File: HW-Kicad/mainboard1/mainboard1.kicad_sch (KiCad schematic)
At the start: 11 parts, among them J1 Conn_01x02_Male, J2 Conn_01x02_Male, J3 Conn_01x07_Male, J4 Conn_01x04_Male, J5 Conn_01x04_Male, U1 MCP1700-2802E_TO92, U2 ESP32-WROOM-E

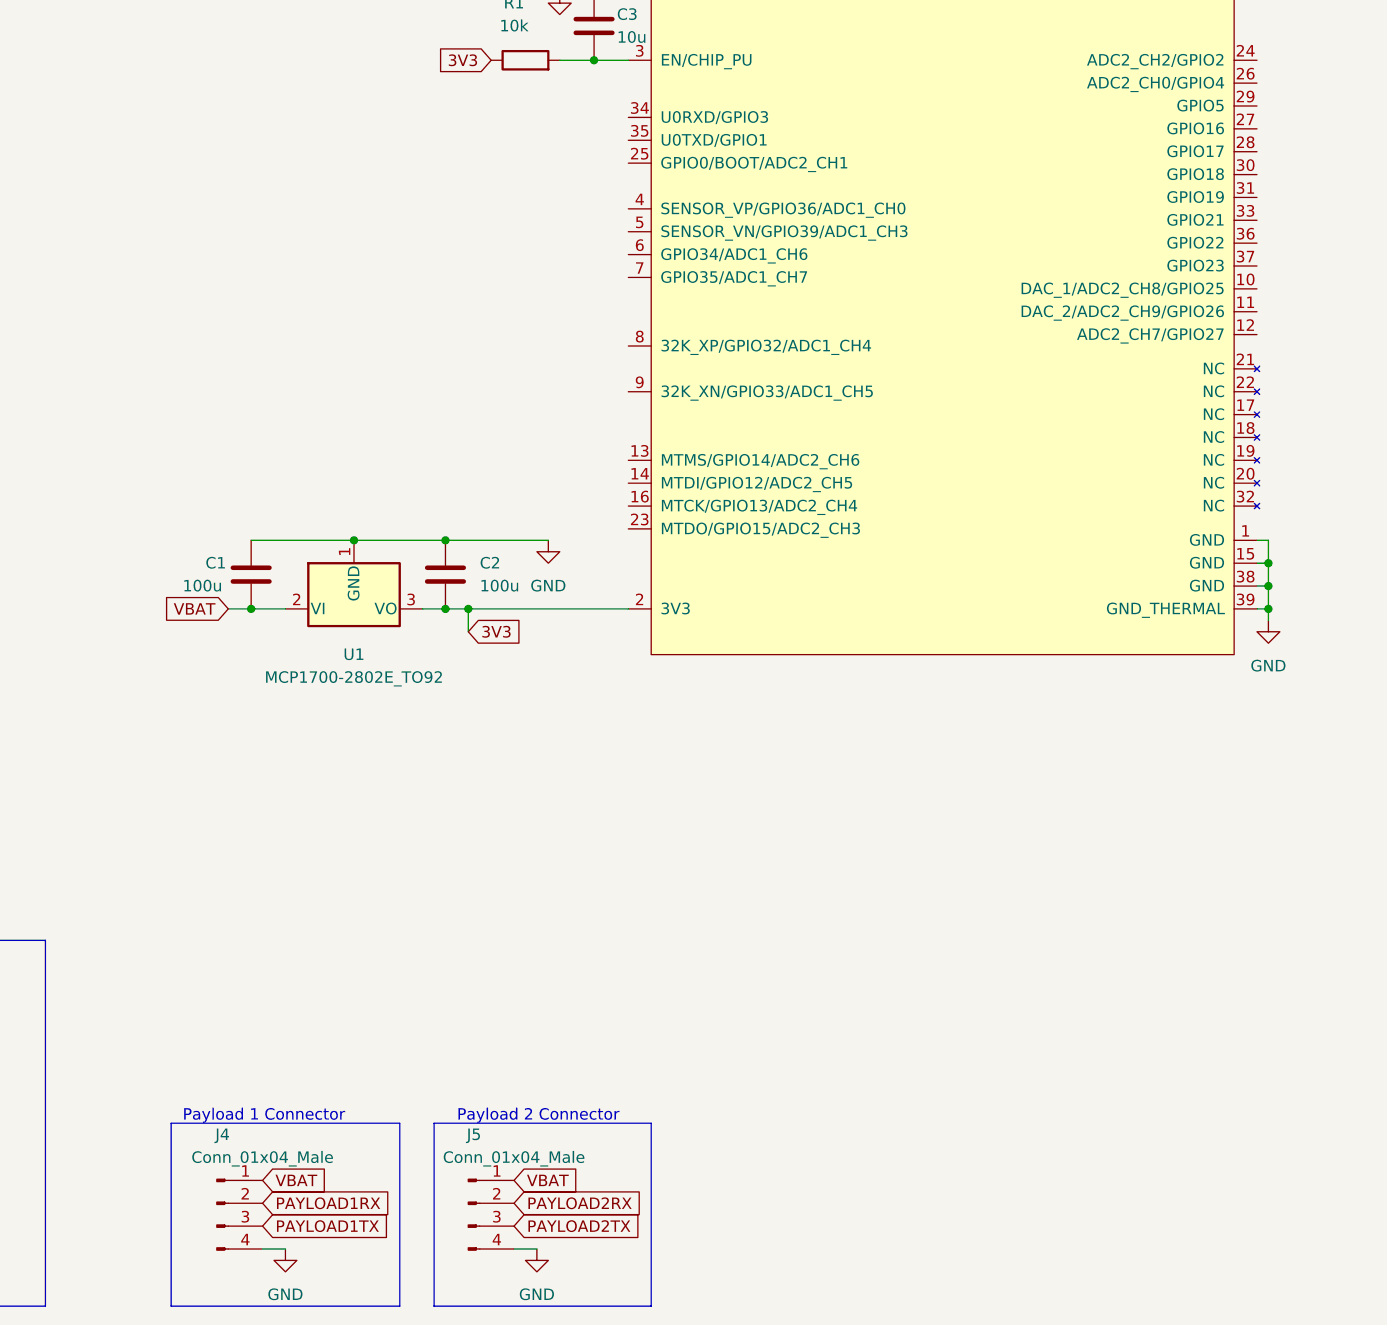
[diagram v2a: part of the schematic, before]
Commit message: falta agregar el mosfet que revienta el globo y el dtmf
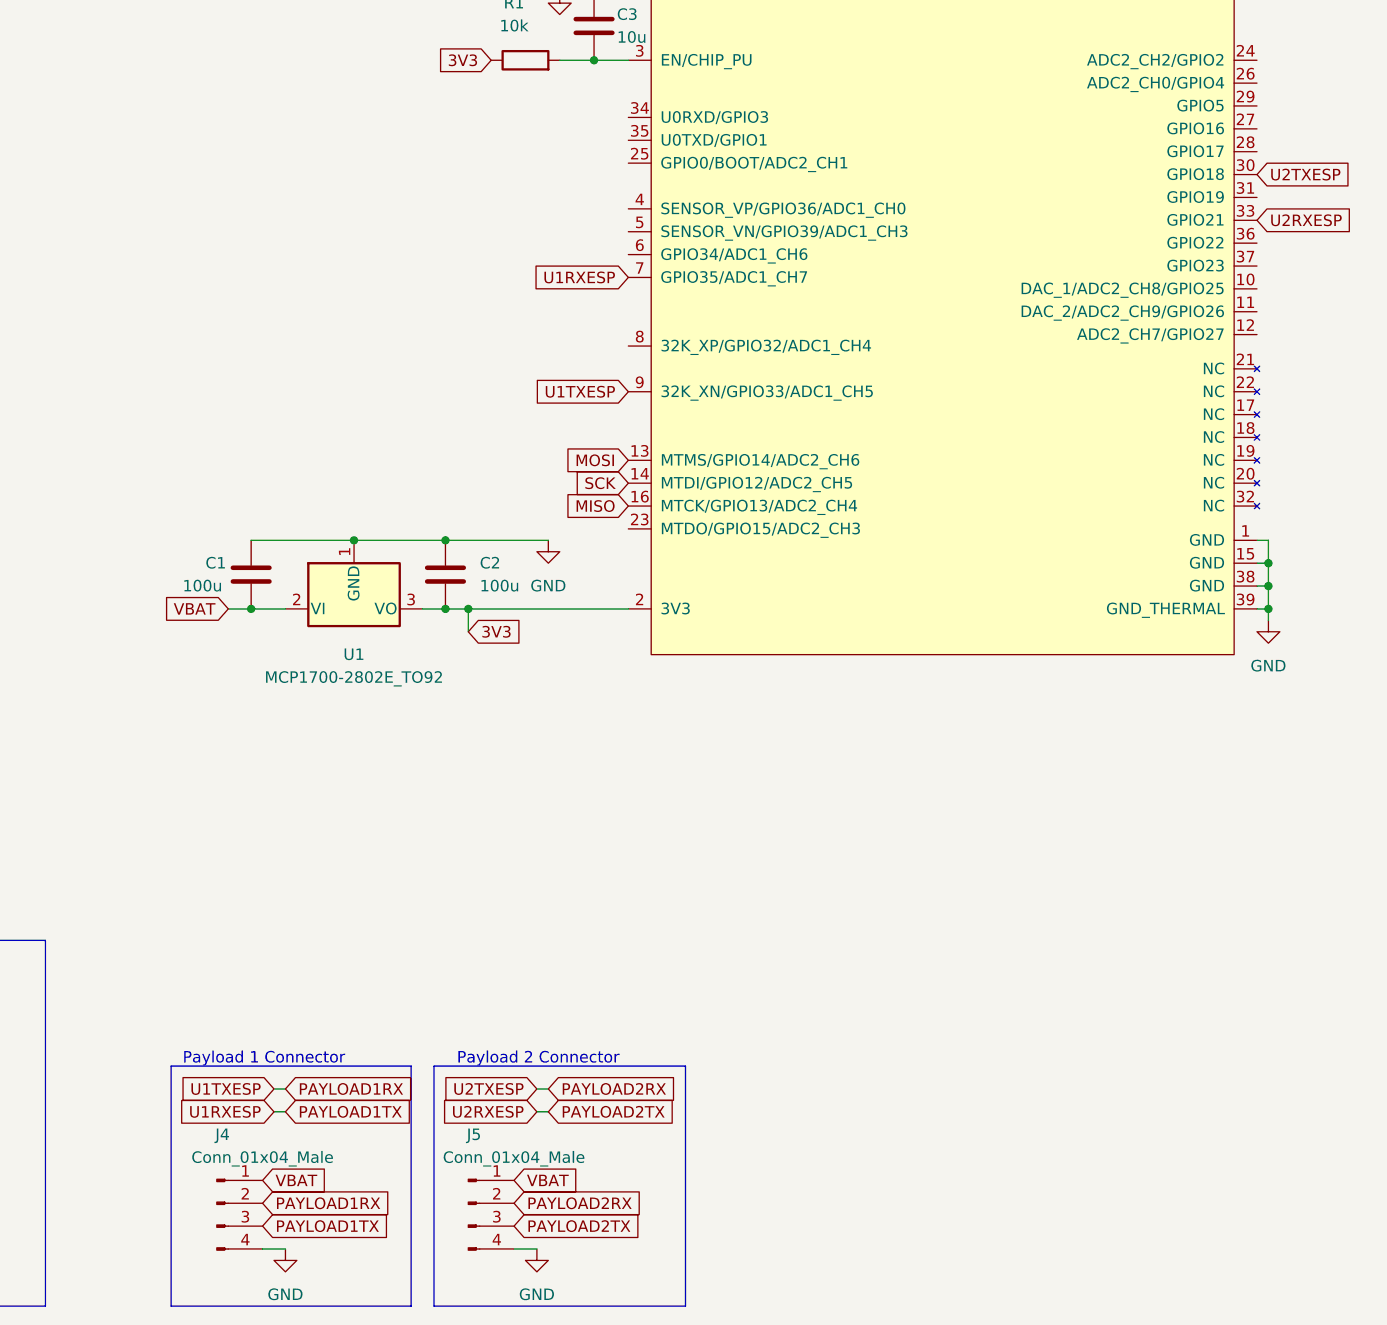
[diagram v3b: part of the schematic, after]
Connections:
- net MISO: now also U2.16 (MTCK/GPIO13/ADC2_CH4)
- net MOSI: now also U2.13 (MTMS/GPIO14/ADC2_CH6)
- net PAYLOAD1RX: now also U2.9 (32K_XN/GPIO33/ADC1_CH5)
- net PAYLOAD1TX: now also U2.7 (GPIO35/ADC1_CH7)
- net PAYLOAD2RX: now also U2.30 (GPIO18)
- net PAYLOAD2TX: now also U2.33 (GPIO21)
- net SCK: now also U2.14 (MTDI/GPIO12/ADC2_CH5)
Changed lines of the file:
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@@
+    (stroke (width 0) (type default) (color 0 0 0 0))
+  )
+  (wire (pts (xy 124.46 167.64) (xy 125.73 167.64))
     (stroke (width 0) (type default) (color 0 0 0 0))
   )
@@
     (stroke (width 0) (type default) (color 0 0 0 0))
   )
+  (wire (pts (xy 95.25 170.18) (xy 96.52 170.18))
+    (stroke (width 0) (type default) (color 0 0 0 0))
+  )
   (wire (pts (xy 205.74 106.68) (xy 205.74 109.22))
     (stroke (width 0) (type default) (color 0 0 0 0))
@@
     (stroke (width 0) (type default) (color 0 0 0 0))
   )
+  (wire (pts (xy 124.46 170.18) (xy 125.73 170.18))
+    (stroke (width 0) (type default) (color 0 0 0 0))
+  )
   (polyline (pts (xy 40.64 31.75) (xy 45.72 31.75))
     (stroke (width 0) (type default) (color 0 0 0 0))
@@
     (stroke (width 0) (type default) (color 0 0 0 0))
   )
-  (polyline (pts (xy 109.22 191.77) (xy 83.82 191.77))
+  (wire (pts (xy 95.25 167.64) (xy 96.52 167.64))
+    (stroke (width 0) (type default) (color 0 0 0 0))
+  )
+  (polyline (pts (xy 110.49 191.77) (xy 83.82 191.77))
     (stroke (width 0) (type default) (color 0 0 0 0))
   )
@@
     (stroke (width 0) (type default) (color 0 0 0 0))
   )
-  (polyline (pts (xy 83.82 171.45) (xy 83.82 191.77))
+  (polyline (pts (xy 83.82 165.1) (xy 83.82 191.77))
     (stroke (width 0) (type default) (color 0 0 0 0))
   )
@@
     (stroke (width 0) (type default) (color 0 0 0 0))
   )
-  (polyline (pts (xy 83.82 171.45) (xy 109.22 171.45))
+  (polyline (pts (xy 83.82 165.1) (xy 110.49 165.1))
     (stroke (width 0) (type default) (color 0 0 0 0))
   )
@@
     (stroke (width 0) (type default) (color 0 0 0 0))
   )
-  (polyline (pts (xy 137.16 191.77) (xy 113.03 191.77))
+  (polyline (pts (xy 140.97 191.77) (xy 113.03 191.77))
     (stroke (width 0) (type default) (color 0 0 0 0))
   )
@@
     (stroke (width 0) (type default) (color 0 0 0 0))
   )
-  (polyline (pts (xy 137.16 171.45) (xy 137.16 191.77))
+  (polyline (pts (xy 140.97 165.1) (xy 140.97 191.77))
     (stroke (width 0) (type default) (color 0 0 0 0))
   )
@@
     (stroke (width 0) (type default) (color 0 0 0 0))
   )
-  (polyline (pts (xy 109.22 171.45) (xy 109.22 191.77))
+  (polyline (pts (xy 110.49 165.1) (xy 110.49 191.77))
     (stroke (width 0) (type default) (color 0 0 0 0))
   )
@@
     (stroke (width 0) (type default) (color 0 0 0 0))
   )
-  (polyline (pts (xy 113.03 171.45) (xy 113.03 191.77))
+  (polyline (pts (xy 113.03 165.1) (xy 113.03 191.77))
     (stroke (width 0) (type default) (color 0 0 0 0))
   )
@@
     (stroke (width 0) (type default) (color 0 0 0 0))
   )
-  (polyline (pts (xy 113.03 171.45) (xy 137.16 171.45))
-    (stroke (width 0) (type default) (color 0 0 0 0))
-  )
-  (text "Payload 1 Connector" (at 85.09 171.45 0)
+  (polyline (pts (xy 113.03 165.1) (xy 140.97 165.1))
+    (stroke (width 0) (type default) (color 0 0 0 0))
+  )
+  (text "Payload 1 Connector" (at 85.09 165.1 0)
     (effects (font (size 1.27 1.27)) (justify left bottom))
   )
@@
     (effects (font (size 1.27 1.27)) (justify left bottom))
   )
-  (text "Payload 2 Connector" (at 115.57 171.45 0)
+  (text "Payload 2 Connector" (at 115.57 165.1 0)
     (effects (font (size 1.27 1.27)) (justify left bottom))
   )
@@
     )
   )
+  (global_label "U1RXESP" (shape input) (at 95.25 170.18 180) (fields_autoplaced)
+    (effects (font (size 1.27 1.27)) (justify right))
+    (property "Intersheet References" "${INTERSHEET_REFS}" (id 0) (at 84.1888 170.2594 0)
+      (effects (font (size 1.27 1.27)) (justify right) hide)
+    )
+  )
   (global_label "3V3" (shape input) (at 116.84 116.84 0) (fields_autoplaced)
     (effects (font (size 1.27 1.27)) (justify left))
@@
     )
   )
+  (global_label "U2RXESP" (shape input) (at 204.47 71.12 0) (fields_autoplaced)
+    (effects (font (size 1.27 1.27)) (justify left))
+    (property "Intersheet References" "${INTERSHEET_REFS}" (id 0) (at 215.5312 71.0406 0)
+      (effects (font (size 1.27 1.27)) (justify left) hide)
+    )
+  )
   (global_label "3V3" (shape input) (at 119.38 53.34 180) (fields_autoplaced)
     (effects (font (size 1.27 1.27)) (justify right))
@@
     )
   )
+  (global_label "U2TXESP" (shape input) (at 204.47 66.04 0) (fields_autoplaced)
+    (effects (font (size 1.27 1.27)) (justify left))
+    (property "Intersheet References" "${INTERSHEET_REFS}" (id 0) (at 215.2288 65.9606 0)
+      (effects (font (size 1.27 1.27)) (justify left) hide)
+    )
+  )
   (global_label "SDA" (shape input) (at 39.37 176.53 0) (fields_autoplaced)
     (effects (font (size 1.27 1.27)) (justify left))
@@
     )
   )
+  (global_label "PAYLOAD1RX" (shape input) (at 96.52 167.64 0) (fields_autoplaced)
+    (effects (font (size 1.27 1.27)) (justify left))
+    (property "Intersheet References" "${INTERSHEET_REFS}" (id 0) (at 110.7864 167.5606 0)
+      (effects (font (size 1.27 1.27)) (justify left) hide)
+    )
+  )
   (global_label "VBAT" (shape input) (at 90.17 114.3 180) (fields_autoplaced)
     (effects (font (size 1.27 1.27)) (justify right))
@@
     )
   )
+  (global_label "MISO" (shape input) (at 134.62 102.87 180) (fields_autoplaced)
+    (effects (font (size 1.27 1.27)) (justify right))
+    (property "Intersheet References" "${INTERSHEET_REFS}" (id 0) (at 127.6107 102.9494 0)
+      (effects (font (size 1.27 1.27)) (justify right) hide)
+    )
+  )
   (global_label "PAYLOAD1TX" (shape input) (at 93.98 182.88 0) (fields_autoplaced)
     (effects (font (size 1.27 1.27)) (justify left))
@@
     )
   )
+  (global_label "PAYLOAD1TX" (shape input) (at 96.52 170.18 0) (fields_autoplaced)
+    (effects (font (size 1.27 1.27)) (justify left))
+    (property "Intersheet References" "${INTERSHEET_REFS}" (id 0) (at 110.4841 170.1006 0)
+      (effects (font (size 1.27 1.27)) (justify left) hide)
+    )
+  )
+  (global_label "U1RXESP" (shape input) (at 134.62 77.47 180) (fields_autoplaced)
+    (effects (font (size 1.27 1.27)) (justify right))
+    (property "Intersheet References" "${INTERSHEET_REFS}" (id 0) (at 123.5588 77.5494 0)
+      (effects (font (size 1.27 1.27)) (justify right) hide)
+    )
+  )
+  (global_label "U2RXESP" (shape input) (at 124.46 170.18 180) (fields_autoplaced)
+    (effects (font (size 1.27 1.27)) (justify right))
+    (property "Intersheet References" "${INTERSHEET_REFS}" (id 0) (at 113.3988 170.2594 0)
+      (effects (font (size 1.27 1.27)) (justify right) hide)
+    )
+  )
   (global_label "VBAT" (shape input) (at 36.83 158.75 0) (fields_autoplaced)
     (effects (font (size 1.27 1.27)) (justify left))
@@
     )
   )
+  (global_label "U1TXESP" (shape input) (at 95.25 167.64 180) (fields_autoplaced)
+    (effects (font (size 1.27 1.27)) (justify right))
+    (property "Intersheet References" "${INTERSHEET_REFS}" (id 0) (at 84.4912 167.7194 0)
+      (effects (font (size 1.27 1.27)) (justify right) hide)
+    )
+  )
+  (global_label "SCK" (shape input) (at 134.62 100.33 180) (fields_autoplaced)
+    (effects (font (size 1.27 1.27)) (justify right))
+    (property "Intersheet References" "${INTERSHEET_REFS}" (id 0) (at 128.4574 100.4094 0)
+      (effects (font (size 1.27 1.27)) (justify right) hide)
+    )
+  )
+  (global_label "U1TXESP" (shape input) (at 134.62 90.17 180) (fields_autoplaced)
+    (effects (font (size 1.27 1.27)) (justify right))
+    (property "Intersheet References" "${INTERSHEET_REFS}" (id 0) (at 123.8612 90.2494 0)
+      (effects (font (size 1.27 1.27)) (justify right) hide)
+    )
+  )
   (global_label "VBAT" (shape input) (at 93.98 177.8 0) (fields_autoplaced)
     (effects (font (size 1.27 1.27)) (justify left))
@@
     )
   )
+  (global_label "U2TXESP" (shape input) (at 124.46 167.64 180) (fields_autoplaced)
+    (effects (font (size 1.27 1.27)) (justify right))
+    (property "Intersheet References" "${INTERSHEET_REFS}" (id 0) (at 113.7012 167.7194 0)
+      (effects (font (size 1.27 1.27)) (justify right) hide)
+    )
+  )
   (global_label "MOSI" (shape input) (at 39.37 184.15 0) (fields_autoplaced)
     (effects (font (size 1.27 1.27)) (justify left))
@@
     )
   )
+  (global_label "PAYLOAD2TX" (shape input) (at 125.73 170.18 0) (fields_autoplaced)
+    (effects (font (size 1.27 1.27)) (justify left))
+    (property "Intersheet References" "${INTERSHEET_REFS}" (id 0) (at 139.6941 170.1006 0)
+      (effects (font (size 1.27 1.27)) (justify left) hide)
+    )
+  )
   (global_label "VBAT" (shape input) (at 33.02 22.86 0) (fields_autoplaced)
     (effects (font (size 1.27 1.27)) (justify left))
@@
     )
   )
+  (global_label "PAYLOAD2RX" (shape input) (at 125.73 167.64 0) (fields_autoplaced)
+    (effects (font (size 1.27 1.27)) (justify left))
+    (property "Intersheet References" "${INTERSHEET_REFS}" (id 0) (at 139.9964 167.5606 0)
+      (effects (font (size 1.27 1.27)) (justify left) hide)
+    )
+  )
+  (global_label "MOSI" (shape input) (at 134.62 97.79 180) (fields_autoplaced)
+    (effects (font (size 1.27 1.27)) (justify right))
+    (property "Intersheet References" "${INTERSHEET_REFS}" (id 0) (at 127.6107 97.8694 0)
+      (effects (font (size 1.27 1.27)) (justify right) hide)
+    )
+  )
